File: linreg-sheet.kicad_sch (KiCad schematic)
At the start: 19 parts, among them J1 PWR_TERM, J2 PWR_TERM, U12 XC6206PxxxMR, U13 XC6206PxxxMR, U16 XC6206PxxxMR, U4 XC6206PxxxMR

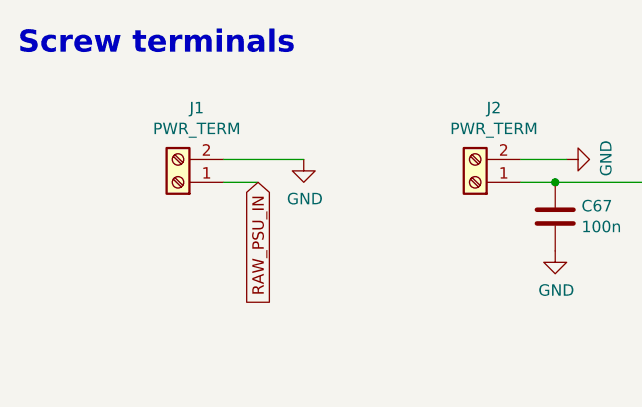
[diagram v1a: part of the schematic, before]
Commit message: powerpole connector, some silk adjustments, holes for pp
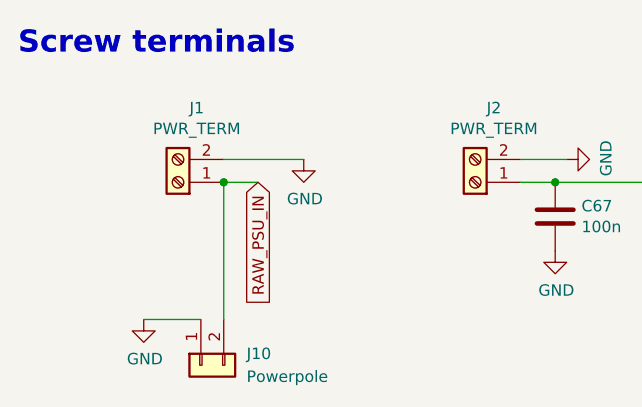
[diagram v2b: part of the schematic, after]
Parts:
- added J10: Powerpole, NPR:PowerPole_PP45_1336G1_1x2_Horizontal, symbol Connector_Generic:Conn_01x02
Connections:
- net GND: now also J10.1 (Pin_1)
- net RAW_PSU_IN: now also J10.2 (Pin_2)
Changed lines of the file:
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@@
   (junction (at 168.91 35.56) (diameter 0) (color 0 0 0 0)
   )
+  (junction (at 86.36 172.72) (diameter 0) (color 0 0 0 0)
+  )
   (junction (at 118.11 127) (diameter 0) (color 0 0 0 0)
   )
@@
     (stroke (width 0) (type default))
   )
+  (wire (pts (xy 86.36 172.72) (xy 86.36 187.96))
+    (stroke (width 0) (type default))
+  )
   (wire (pts (xy 144.78 97.79) (xy 156.21 97.79))
     (stroke (width 0) (type default))
@@
   )
   (wire (pts (xy 138.43 172.72) (xy 123.19 172.72))
+    (stroke (width 0) (type default))
+  )
+  (wire (pts (xy 77.47 187.96) (xy 83.82 187.96))
     (stroke (width 0) (type default))
   )
@@
         )
       )
+    )
+  )
+  (symbol (lib_id "power:GND") (at 77.47 187.96 0) (unit 1)
+    (in_bom yes) (on_board yes) (dnp no)
+    (property "Reference" "#PWR02" (at 77.47 194.31 0)
+      (effects (font (size 1.27 1.27)) hide)
+    )
+    (property "Value" "GND" (at 77.597 192.3542 0)
+      (effects (font (size 1.27 1.27)))
+    )
+    (property "Footprint" "" (at 77.47 187.96 0)
+      (effects (font (size 1.27 1.27)) hide)
+    )
+    (property "Datasheet" "" (at 77.47 187.96 0)
+      (effects (font (size 1.27 1.27)) hide)
+    )
+    (pin "1")
+    (instances
+      (project "TACNPR"
+        (path "/9538e4ed-27e6-4c37-b989-9859dc0d49e8/00000000-0000-0000-0000-0000607fb7f8"
+          (reference "#PWR02") (unit 1)
+        )
+      )
+    )
+  )
+  (symbol (lib_id "Connector_Generic:Conn_01x02") (at 83.82 193.04 90) (mirror x) (unit 1)
+    (in_bom yes) (on_board yes) (dnp no) (fields_autoplaced)
+    (property "Reference" "J10" (at 88.9 191.77 90)
+      (effects (font (size 1.27 1.27)) (justify right))
+    )
+    (property "Value" "Powerpole" (at 88.9 194.31 90)
+      (effects (font (size 1.27 1.27)) (justify right))
+    )
+    (property "Footprint" "NPR:PowerPole_PP45_1336G1_1x2_Horizontal" (at 83.82 193.04 0)
+      (effects (font (size 1.27 1.27)) hide)
+    )
+    (property "Datasheet" "~" (at 83.82 193.04 0)
+      (effects (font (size 1.27 1.27)) hide)
+    )
+    (pin "2")
+    (pin "1")
+    (instances
+      (project "TACNPR"
+        (path "/9538e4ed-27e6-4c37-b989-9859dc0d49e8/00000000-0000-0000-0000-0000607fb7f8"
+          (reference "J10") (unit 1)
+        )
+      )

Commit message: some notes to schema on PP strain relief
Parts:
- J10: symbol Connector_Generic:Conn_01x02 -> Connector_Generic:Conn_01x05
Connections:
- net GND: now also J10.3 (Pin_3), J10.4 (Pin_4), J10.5 (Pin_5)
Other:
- note added: "DC power can be fed either using screw terminal or Anderson Powerpole connector (7,9mm pitch)"
- note added: "Powerpole strain relief options: 1) solder a wire around it into GND pads 3 and 4 2) use the mounting hole (machine screw and nut)"
- note added: "Screw terminals (power in and 12V DC out)"
- note removed: "Screw terminals"
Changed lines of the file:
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@@
   (junction (at 167.64 66.04) (diameter 0) (color 0 0 0 0)
   )
+  (junction (at 93.98 187.96) (diameter 0) (color 0 0 0 0)
+  )
   (junction (at 167.64 97.79) (diameter 0) (color 0 0 0 0)
   )
@@
   (junction (at 156.21 127) (diameter 0) (color 0 0 0 0)
   )
+  (junction (at 91.44 187.96) (diameter 0) (color 0 0 0 0)
+  )
   (junction (at 123.19 172.72) (diameter 0) (color 0 0 0 0)
   )
@@
     (stroke (width 0) (type default))
   )
+  (wire (pts (xy 91.44 187.96) (xy 93.98 187.96))
+    (stroke (width 0) (type default))
+  )
   (wire (pts (xy 106.68 35.56) (xy 119.38 35.56))
     (stroke (width 0) (type default))
@@
     (stroke (width 0) (type default))
   )
+  (wire (pts (xy 88.9 187.96) (xy 91.44 187.96))
+    (stroke (width 0) (type default))
+  )
   (wire (pts (xy 119.38 66.04) (xy 129.54 66.04))
     (stroke (width 0) (type default))
@@
     (stroke (width 0) (type default))
   )
+  (wire (pts (xy 93.98 187.96) (xy 97.79 187.96))
+    (stroke (width 0) (type default))
+  )
   (wire (pts (xy 138.43 172.72) (xy 123.19 172.72))
     (stroke (width 0) (type default))
@@
     (stroke (width 0) (type default))
   )
-  (text "Screw terminals" (at 63.5 158.75 0)
+  (text "Screw terminals (power in and 12V DC out)" (at 63.5 158.75 0)
     (effects (font (size 2.4638 2.4638) (thickness 0.4928) bold) (justify left bottom))
   )
   (text "3V3 for \nSTM32 CPU" (at 63.5 71.12 0)
     (effects (font (size 2.4638 2.4638) (thickness 0.4928) bold) (justify left bottom))
+  )
+  (text "DC power can be fed \neither using screw terminal \nor Anderson Powerpole \nconnector (7,9mm pitch)"
+    (at 33.02 182.88 0)
+    (effects (font (size 2.0038 2.0038) (thickness 0.4008) bold) (justify left bottom))
   )
   (text "TACNPR / regulators & terminals" (at 180.34 173.99 0)
@@
     (at 180.34 179.07 0)
     (effects (font (size 2.4892 2.4892) (thickness 0.4978) bold italic) (justify left bottom))
+  )
+  (text "Powerpole strain relief options: \n1) solder a wire around it into GND pads 3 and 4\n2) use the mounting hole (machine screw and nut)"
+    (at 104.14 195.58 0)
+    (effects (font (size 1.5 1.5) (thickness 0.2008) bold) (justify left bottom))
   )
   (global_label "3V8_OUT" (shape input) (at 106.68 35.56 180) (fields_autoplaced)
@@
     )
   )
-  (symbol (lib_id "Connector_Generic:Conn_01x02") (at 83.82 193.04 90) (mirror x) (unit 1)
-    (in_bom yes) (on_board yes) (dnp no) (fields_autoplaced)
-    (property "Reference" "J10" (at 88.9 191.77 90)
-      (effects (font (size 1.27 1.27)) (justify right))
-    )
-    (property "Value" "Powerpole" (at 88.9 194.31 90)
-      (effects (font (size 1.27 1.27)) (justify right))
-    )
-    (property "Footprint" "NPR:PowerPole_PP45_1336G1_1x2_Horizontal" (at 83.82 193.04 0)
-      (effects (font (size 1.27 1.27)) hide)
-    )
-    (property "Datasheet" "~" (at 83.82 193.04 0)
-      (effects (font (size 1.27 1.27)) hide)
-    )
-    (pin "2")
-    (pin "1")
+  (symbol (lib_id "Connector_Generic:Conn_01x05") (at 88.9 193.04 90) (mirror x) (unit 1)
+    (in_bom yes) (on_board yes) (dnp no)
+    (property "Reference" "J10" (at 83.82 195.58 90)
+      (effects (font (size 1.27 1.27)))
+    )
+    (property "Value" "Powerpole" (at 91.44 195.58 90)
+      (effects (font (size 1.27 1.27)))
+    )
+    (property "Footprint" "NPR:PowerPole_PP45_1336G1_1x2_Horizontal" (at 88.9 193.04 0)
+      (effects (font (size 1.27 1.27)) hide)
+    )
+    (property "Datasheet" "~" (at 88.9 193.04 0)
+      (effects (font (size 1.27 1.27)) hide)
+    )
+    (pin "2")
+    (pin "1")
+    (pin "3")
+    (pin "4")
+    (pin "5")
     (instances
       (project "TACNPR"
@@
         )
       )
+    )
+  )
+  (symbol (lib_id "power:GND") (at 97.79 187.96 0) (unit 1)
+    (in_bom yes) (on_board yes) (dnp no)
+    (property "Reference" "#PWR03" (at 97.79 194.31 0)
+      (effects (font (size 1.27 1.27)) hide)
+    )
+    (property "Value" "GND" (at 97.917 192.3542 0)
+      (effects (font (size 1.27 1.27)))
+    )
+    (property "Footprint" "" (at 97.79 187.96 0)
+      (effects (font (size 1.27 1.27)) hide)
+    )
+    (property "Datasheet" "" (at 97.79 187.96 0)
+      (effects (font (size 1.27 1.27)) hide)
+    )
+    (pin "1")
+    (instances
+      (project "TACNPR"
+        (path "/9538e4ed-27e6-4c37-b989-9859dc0d49e8/00000000-0000-0000-0000-0000607fb7f8"
+          (reference "#PWR03") (unit 1)
+        )
+      )

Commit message: update DNP to pwr in connector
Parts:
- J1: DNP (none) -> true
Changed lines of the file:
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@@
+			)
+		)
+		(property "DNP" "true"
+			(at 81.28 172.72 0)
+			(effects
+				(font
+					(size 5.0038 5.0038)
+				)
+				(hide yes)
 			)
 		)
